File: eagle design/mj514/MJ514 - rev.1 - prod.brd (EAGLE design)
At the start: 49 x 18 mm, 14 parts, among them IC202 LDK320AM33R, IC302 STM32F042G6U6, IC401 TCAN334

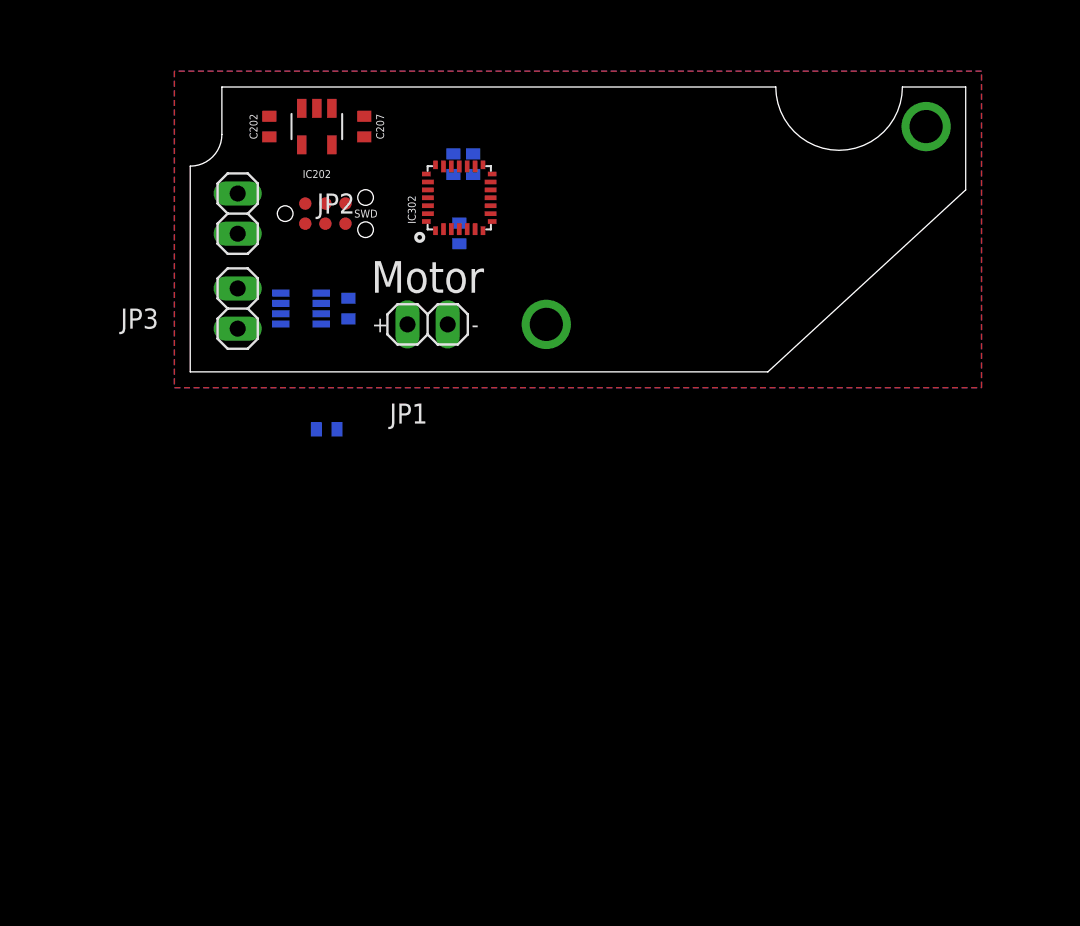
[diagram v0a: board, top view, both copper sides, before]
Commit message: MJ818 SuperNova Mini2: - added position key into PCB and spacers; updated gerber, dwg and stl
mj513 - grip:
- corrected bushing dimensions

in mj8x8-foo:
- minor corrections

general board-wide effort:
- replaced pinhead with 0.9mm TH
- added 2nd CAN H & L solder contact
- unified sch nets and drawings

in mj8x8 foo:
- developed rev.1b mj-foo device with voltage detector and CAN TVS protection

in mj808 design:
- updated front led shunt resistor to 0.18 Ohm

in mj8x8:
- added HR30-6R-6P - PushPull Receptacle.lbr receptable
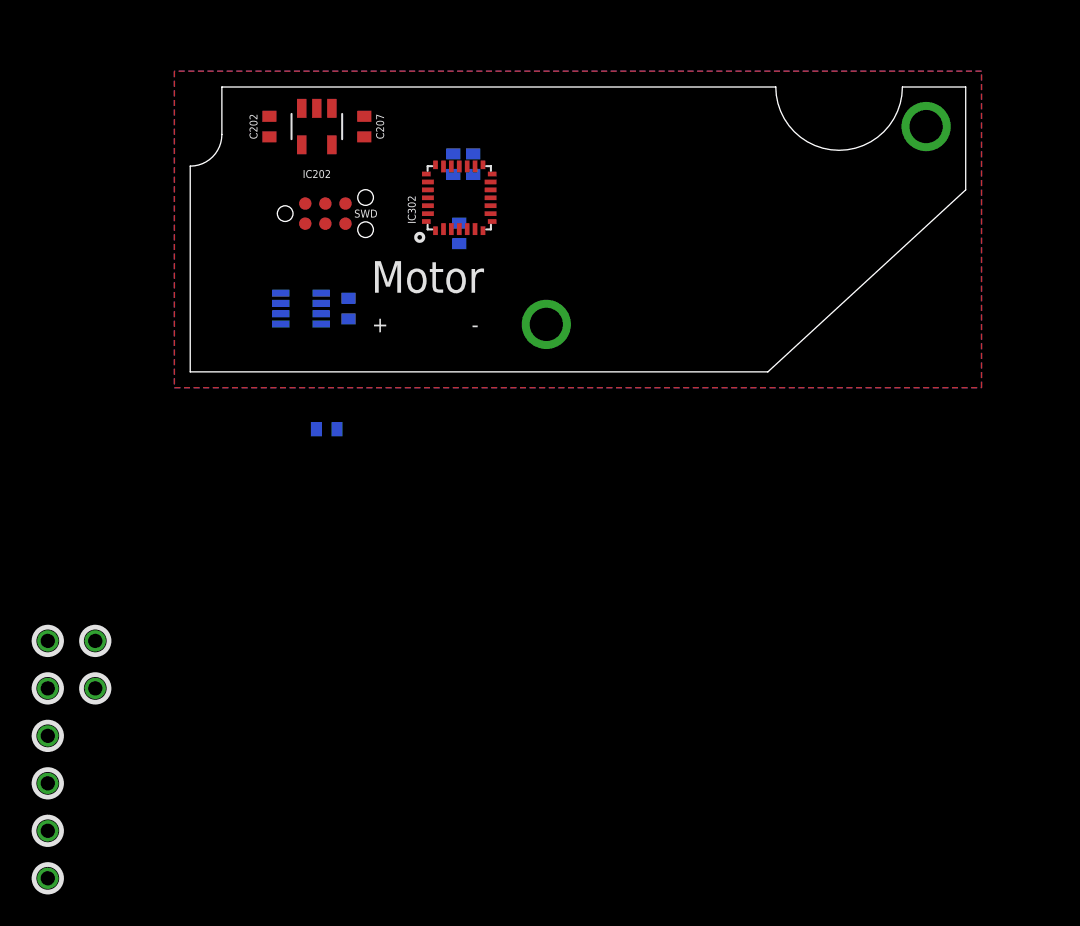
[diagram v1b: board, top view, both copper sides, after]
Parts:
- removed JP1, JP2, JP3: (no value), pinhead:1X02
- added TP1: LiIon + Terminal, signal testpoint:TH-0.9
- added TP2: LiIon - Terminal, signal testpoint:TH-0.9
- added TP3: motor +, signal testpoint:TH-0.9
- added TP4: motor -, signal testpoint:TH-0.9
- added TP5, TP7: CAN high, signal testpoint:TH-0.9
- added TP6, TP8: CAN low, signal testpoint:TH-0.9
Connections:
- net BAT+: now also TP1.P$1; no longer JP2.2
- net CAN_H: now also TP5.P$1, TP7.P$1; no longer JP3.1
- net CAN_L: now also TP6.P$1, TP8.P$1; no longer JP3.2
- net GND: now also TP2.P$1; no longer JP2.1
- net MOTOR+: now also TP3.P$1; no longer JP1.1
- net MOTOR-: now also TP4.P$1; no longer JP1.2
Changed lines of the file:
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@@
 </variantdefs>
 <classes>
-<class number="0" name="GND" width="0" drill="0">
+<class number="0" name="GND" width="0.25" drill="0.35">
+<clearance class="0" value="0.19"/>
 </class>
 <class number="1" name="BAT+" width="0.5" drill="0.35">
@@
 <attribute name="VALUE" x="7" y="4" size="0.5" layer="28" font="vector" rot="MR0" align="center"/>
 </element>
-<element name="JP1" library="pinhead" library_urn="urn:adsk.eagle:library:325" package="1X02" package3d_urn="urn:adsk.eagle:package:22435/2" value="" x="15" y="3" smashed="yes">
-<attribute name="NAME" x="15" y="-2" size="1.27" layer="25" ratio="10" rot="R180"/>
-<attribute name="POPULARITY" value="98" x="15" y="3" size="1.778" layer="27" display="off"/>
-<attribute name="VALUE" x="12.46" y="-0.175" size="1.27" layer="27"/>
-</element>
-<element name="JP2" library="pinhead" library_urn="urn:adsk.eagle:library:325" package="1X02" package3d_urn="urn:adsk.eagle:package:22435/2" value="" x="3" y="10" smashed="yes" rot="R90">
-<attribute name="NAME" x="8" y="10" size="1.27" layer="25" ratio="10"/>
-<attribute name="POPULARITY" value="98" x="3" y="10" size="1" layer="27" font="vector" rot="R90" display="off"/>
-<attribute name="VALUE" x="6.175" y="7.46" size="1.27" layer="27" rot="R90"/>
-</element>
-<element name="JP3" library="pinhead" library_urn="urn:adsk.eagle:library:325" package="1X02" package3d_urn="urn:adsk.eagle:package:22435/2" value="" x="3" y="4" smashed="yes" rot="R270">
-<attribute name="NAME" x="-2" y="4" size="1.27" layer="25" ratio="10" rot="R180"/>
-<attribute name="POPULARITY" value="98" x="3" y="4" size="1" layer="27" font="vector" rot="R270" display="off"/>
-<attribute name="VALUE" x="-0.175" y="6.54" size="1.27" layer="27" rot="R270"/>
-</element>
 <element name="SWD1" library="tag-connect" package="TC2030-NL" value="" x="6" y="10" smashed="yes"/>
+<element name="TP5" library="signal testpoint" package="TH-0.9" value="CAN high" x="-9" y="-17" smashed="yes"/>
+<element name="TP6" library="signal testpoint" package="TH-0.9" value="CAN low" x="-6" y="-17" smashed="yes"/>
+<element name="TP7" library="signal testpoint" package="TH-0.9" value="CAN high" x="-9" y="-20" smashed="yes"/>
+<element name="TP8" library="signal testpoint" package="TH-0.9" value="CAN low" x="-6" y="-20" smashed="yes"/>
+<element name="TP2" library="signal testpoint" package="TH-0.9" value="LiIon - Terminal" x="-9" y="-26" smashed="yes"/>
+<element name="TP1" library="signal testpoint" package="TH-0.9" value="LiIon + Terminal" x="-9" y="-23" smashed="yes"/>
+<element name="TP3" library="signal testpoint" package="TH-0.9" value="motor +" x="-9" y="-29" smashed="yes"/>
+<element name="TP4" library="signal testpoint" package="TH-0.9" value="motor -" x="-9" y="-32" smashed="yes"/>
 </elements>
 <signals>
@@
 <via x="22.5" y="3" extent="1-16" drill="2.1"/>
 <via x="46.5" y="15.5" extent="1-16" drill="2.1"/>
-<contactref element="JP2" pad="1"/>
 <contactref element="SWD1" pad="5_GND"/>
-<wire x1="17" y1="9.4" x2="9.275" y2="-3.625" width="0" layer="19" extent="1-1"/>
-<wire x1="16.625" y1="12.475" x2="17" y2="9.4" width="0" layer="19" extent="1-1"/>
-<wire x1="17.875" y1="12.475" x2="16.625" y2="12.475" width="0" layer="19" extent="1-1"/>
-<wire x1="8.275" y1="4.325" x2="17.875" y2="12.475" width="0" layer="19" extent="1-16"/>
-<wire x1="10" y1="4.65" x2="8.275" y2="4.325" width="0" layer="19" extent="16-16"/>
-<wire x1="9.81" y1="9.365" x2="8.275" y2="4.325" width="0" layer="19" extent="1-16"/>
+<contactref element="TP2" pad="P$1"/>
+<wire x1="22.5" y1="3" x2="46.5" y2="15.5" width="0" layer="19" extent="1-1"/>
+<wire x1="17" y1="9.4" x2="22.5" y2="3" width="0" layer="19" extent="16-16"/>
+<wire x1="16.625" y1="12.475" x2="17" y2="9.4" width="0" layer="19" extent="16-16"/>
+<wire x1="17.875" y1="12.475" x2="16.625" y2="12.475" width="0" layer="19" extent="16-16"/>
+<wire x1="18" y1="12.98" x2="17.875" y2="12.475" width="0" layer="19" extent="1-16"/>
+<wire x1="11" y1="16.15" x2="16.625" y2="12.475" width="0" layer="19" extent="1-16"/>
+<wire x1="8" y1="16.65" x2="11" y2="16.15" width="0" layer="19" extent="1-1"/>
+<wire x1="5" y1="14.85" x2="8" y2="16.65" width="0" layer="19" extent="1-1"/>
+<wire x1="9.81" y1="9.365" x2="11" y2="16.15" width="0" layer="19" extent="1-1"/>
+<wire x1="10" y1="4.65" x2="9.81" y2="9.365" width="0" layer="19" extent="1-16"/>
+<wire x1="8.275" y1="4.325" x2="10" y2="4.65" width="0" layer="19" extent="16-16"/>
+<wire x1="9.275" y1="-3.625" x2="8.275" y2="4.325" width="0" layer="19" extent="16-16"/>
+<wire x1="-9" y1="-26" x2="9.275" y2="-3.625" width="0" layer="19" extent="16-16"/>
 </signal>
 <signal name="BAT+" class="1">
@@
 <contactref element="IC202" pad="IN"/>
 <contactref element="C202" pad="1"/>
-<contactref element="JP2" pad="2"/>
-<wire x1="7.05" y1="16.65" x2="8.95" y2="16.65" width="0" layer="19" extent="1-1"/>
-<wire x1="5" y1="16.15" x2="7.05" y2="16.65" width="0" layer="19" extent="1-1"/>
-<wire x1="3" y1="11.27" x2="5" y2="16.15" width="0" layer="19" extent="1-1"/>
+<contactref element="TP1" pad="P$1"/>
+<wire x1="5" y1="16.15" x2="-9" y2="-23" width="0" layer="19" extent="1-1"/>
+<wire x1="7.05" y1="16.65" x2="5" y2="16.15" width="0" layer="19" extent="1-1"/>
+<wire x1="8.95" y1="16.65" x2="7.05" y2="16.65" width="0" layer="19" extent="1-1"/>
 </signal>
 <signal name="CAN_H" class="3">
 <contactref element="IC401" pad="P$7"/>
-<contactref element="JP3" pad="1"/>
-<wire x1="3" y1="5.27" x2="5.725" y2="4.325" width="0" layer="19" extent="16-16"/>
+<contactref element="TP5" pad="P$1"/>
+<contactref element="TP7" pad="P$1"/>
+<wire x1="-9" y1="-17" x2="-9" y2="-20" width="0" layer="19" extent="1-1"/>
+<wire x1="5.725" y1="4.325" x2="-9" y2="-17" width="0" layer="19" extent="16-16"/>
 </signal>
 <signal name="CAN_L" class="3">
 <contactref element="IC401" pad="P$6"/>
-<contactref element="JP3" pad="2"/>
-<wire x1="3" y1="2.73" x2="5.725" y2="3.675" width="0" layer="19" extent="16-16"/>
+<contactref element="TP8" pad="P$1"/>
+<contactref element="TP6" pad="P$1"/>
+<wire x1="-6" y1="-17" x2="-6" y2="-20" width="0" layer="19" extent="1-1"/>
+<wire x1="5.725" y1="3.675" x2="-6" y2="-17" width="0" layer="19" extent="16-16"/>
 </signal>
 <signal name="3V3" class="4">
+<contactref element="C405" pad="1"/>
+<contactref element="IC401" pad="P$3"/>
 <contactref element="IC202" pad="OUT"/>
 <contactref element="C207" pad="2"/>
@@
 <contactref element="C304" pad="2"/>
 <contactref element="C305" pad="2"/>
-<contactref element="C405" pad="1"/>
-<contactref element="IC401" pad="P$3"/>
 <contactref element="SWD1" pad="1_TVCC"/>
-<wire x1="16.625" y1="13.775" x2="17" y2="8.1" width="0" layer="19" extent="1-1"/>
-<wire x1="17.875" y1="13.775" x2="16.625" y2="13.775" width="0" layer="19" extent="1-1"/>
-<wire x1="10" y1="3.35" x2="17.875" y2="13.775" width="0" layer="19" extent="1-16"/>
-<wire x1="8.275" y1="3.675" x2="10" y2="3.35" width="0" layer="19" extent="16-16"/>
-<wire x1="7.27" y1="9.365" x2="8.275" y2="3.675" width="0" layer="19" extent="1-16"/>
-<wire x1="8.95" y1="14.35" x2="7.27" y2="9.365" width="0" layer="19" extent="1-1"/>
-<wire x1="11" y1="14.85" x2="8.95" y2="14.35" width="0" layer="19" extent="1-1"/>
-<wire x1="17" y1="12.98" x2="11" y2="14.85" width="0" layer="19" extent="1-1"/>
-<wire x1="17.5" y1="12.98" x2="17" y2="12.98" width="0" layer="19" extent="1-1"/>
+<wire x1="17.5" y1="12.98" x2="17.875" y2="13.775" width="0" layer="19" extent="1-16"/>
+<wire x1="17" y1="12.98" x2="17.5" y2="12.98" width="0" layer="19" extent="1-1"/>
+<wire x1="16.625" y1="13.775" x2="17" y2="12.98" width="0" layer="19" extent="1-16"/>
 <wire x1="17.5" y1="9.02" x2="17.5" y2="12.98" width="0" layer="19" extent="1-1"/>
+<wire x1="17" y1="8.1" x2="17.5" y2="9.02" width="0" layer="19" extent="1-16"/>
+<wire x1="11" y1="14.85" x2="16.625" y2="13.775" width="0" layer="19" extent="1-16"/>
+<wire x1="8.95" y1="14.35" x2="11" y2="14.85" width="0" layer="19" extent="1-1"/>
+<wire x1="7.27" y1="9.365" x2="8.95" y2="14.35" width="0" layer="19" extent="1-1"/>
+<wire x1="8.275" y1="3.675" x2="7.27" y2="9.365" width="0" layer="19" extent="1-16"/>
+<wire x1="10" y1="3.35" x2="8.275" y2="3.675" width="0" layer="19" extent="16-16"/>
 </signal>
 <signal name="SYS_SWDIO" class="3">
@@
 </polygon>
 </signal>
-<signal name="MOTOR+">
-<contactref element="JP1" pad="1"/>
-</signal>
-<signal name="MOTOR-">
-<contactref element="JP1" pad="2"/>
+<signal name="MOTOR+" class="5">
+<contactref element="TP3" pad="P$1"/>
+</signal>
+<signal name="MOTOR-" class="5">
+<contactref element="TP4" pad="P$1"/>
 </signal>
 </signals>

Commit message: mj514 prod work: - essentially copied POC sch & brd - added SHT40-AD1F - Humidity Sensor to POC and prod boards - converted to 6 layer board - ERC & DRC check out ok - created gerbers
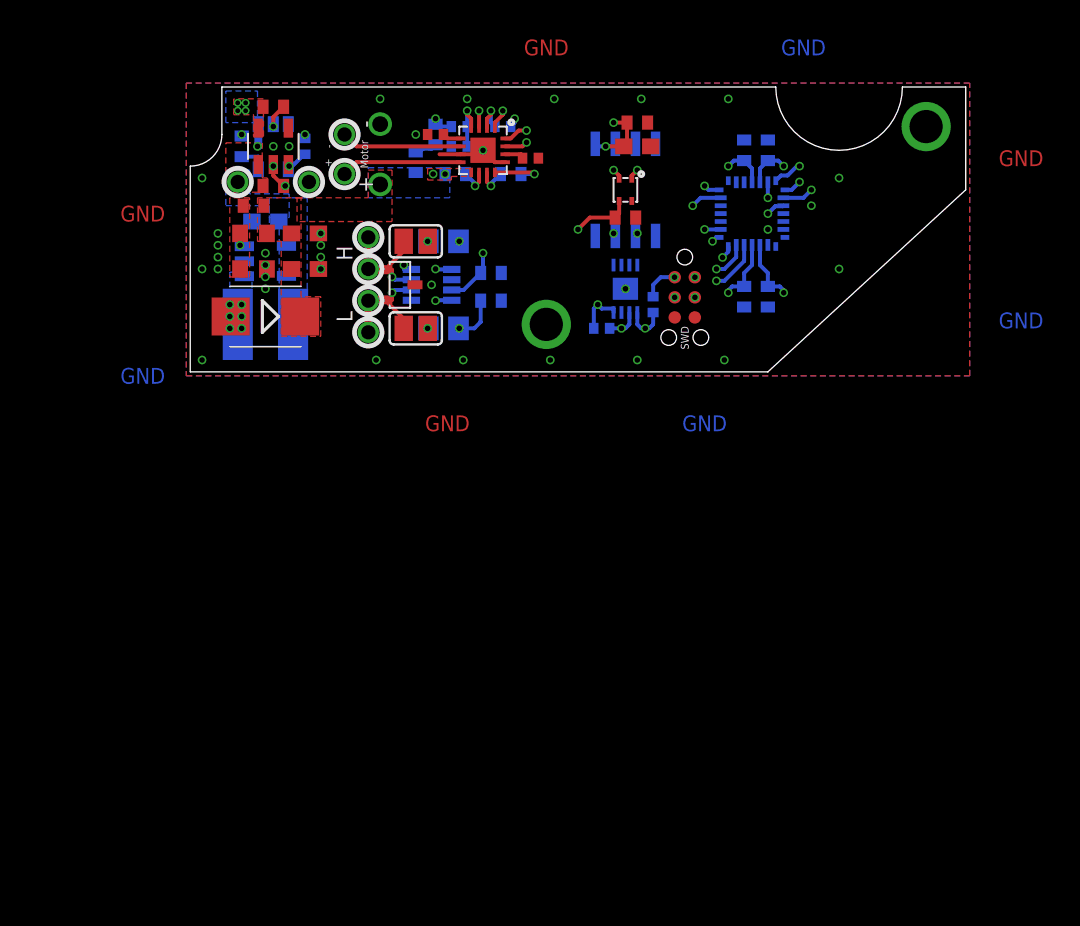
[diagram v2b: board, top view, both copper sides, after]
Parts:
- removed C202, C207: 1uF / 10V, rcl:C0402
- removed IC202: LDK320AM33R, LDK320 5V LDO:SOT-23-5L
- added C201, C203, C204, C701: 1uF / 10V, rcl:C0402
- added C402: 47nF / 10V, rcl:C0402
- added C501, C902, C903, C904: 0.1uF / 100V, rcl:C0402
- added C702, C801, C804: 10uF / 35V, rcl:C0603
- added C802: 4.7uF / 50V, rcl:C0603
- added C803: 68pF / 50V, rcl:C0402
- added C901: 22nF / 50V, rcl:C0402
- added C906: 100uF / 25V, C-Pol:TH
- added D801: MBRM120LT3G, diode:SMB
- added IC201: LDK320AM33R, LDK320 5V LDO:SOT-23-5L
- added IC203: R3119N058A-TR-FE, R3119x - Input Voltage Detector:SOT23-5
- added IC402: SZNUP2105LT1G, NUP2105L - 27V ESD Protection Diode:SOT-23-3
- added IC501: SHT40-AD1F-R2, SHT40-AD1F - Humidity Sensor:SMD
- added IC601: MB85RC16PN-G-AMERE1, MB85RC - FeRAM, I2C:SON-8
- added IC701: AS5601-ASOM, AS5601 - Programmable Contactless Encoder:SOIC8
- added IC801: LT1935ES5#TRMPBF, LTC1935 - Boost DC-DC Converter:TSOT-23-5
- added IC901: DRV8876RGTR, DRV8876 - H-Bridge Motor Driver:VQFN16
- added L801: CDRH4D18NP-4R7NC, CDRH4D18 - Power Inductor:5050
- added R1, R2: 4k7, rcl:R0402
- added R201: 100k, rcl:R0402
- added R402, R403: 60R, 0.5W, rcl:R0805
- added R801: 10k, rcl:R0603
- added R802: 85.6k, rcl:R0603
- added R901, R902: foo, rcl:R0402
- added R903: 10k, rcl:R0402
- added R905: 2.2k, rcl:R0402
- added R906: 1k, rcl:R0402
- added SJ401: CAN H term., jumper:SJ
- added SJ402: CAN L term., jumper:SJ
- C301, C305, C307, C405: value 0.1uF / 10V -> 0.1uF / 100V
- TP3: value motor + -> CAN high
- TP4: value motor - -> CAN high
- TP5: value CAN high -> CAN low
- TP7: value CAN high -> motor +
- TP8: value CAN low -> motor -
- moved TP4 45.3 mm to (11.2, 8.50), turned to 90 degrees
- moved TP2 41.4 mm to (7.50, 12.0), turned to 180 degrees
- moved TP3 40.9 mm to (11.2, 6.50), turned to 90 degrees
- moved TP7 39.7 mm to (9.75, 15.0)
- moved TP1 37.0 mm to (3.00, 12.0), turned to 180 degrees
- moved TP8 36.1 mm to (9.75, 12.5)
- moved C307 31.7 mm to (35.0, 14.0), turned to 270 degrees
- moved TP5 28.1 mm to (11.2, 2.50), turned to 90 degrees
- moved TP6 27.6 mm to (11.2, 4.50), turned to 90 degrees
- moved SWD1 25.4 mm to (31.2, 7.25), turned to 270 degrees
- moved C301 20.4 mm to (36.5, 4.75)
- moved C304 20.2 mm to (36.5, 14.0)
- moved C305 20.2 mm to (35.0, 4.75)
- moved IC302 18.5 mm to (35.5, 10.0), flipped to the bottom, turned to 270 degrees
- moved C405 9.28 mm to (19.0, 6.25), turned to 180 degrees
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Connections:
- new net 12V: C801.1, C803.1, C804.1, C902.2, C903.2, C906.POS, D801.C, IC901.P$9, R802.2
- new net 12V0:FB: C803.2, IC801.FB, R801.2, R802.1
- new net 12V0:SW: D801.A, IC801.SW, L801.P$2
- new net CAN_INFRA:H: R403.2, SJ401.2
- new net CAN_INFRA:L: R402.1, SJ402.2
- new net CAN_INFRA:SPLIT: C402.1, R402.2, R403.1
- new net FE-RAM:WP: IC601.P$7
- new net I2C_SCL: IC302.27_PB6, IC501.SCL, IC601.P$6, IC701.P$7, R1.1
- new net I2C_SDA: IC302.28_PB7, IC501.SDA, IC601.P$5, IC701.P$6, R2.1
- new net MC:CPH: C901.1, IC901.P$11
- new net MC:CPL: C901.2, IC901.P$12
- new net MC:IMODE: IC901.P$5, R901.2
- new net MC:IPROPI: IC901.P$4, R905.2, R906.2
- new net MC:PMODE: IC901.P$14, R902.2
- new net MC:VCP: C902.1, IC901.P$10
- new net MOTOR_FLT: IC302.8_PA2, IC901.P$2, R903.1
- new net MOTOR_IN1: IC302.6_PA0, IC901.P$15
- new net MOTOR_IN2: IC302.7_PA1, IC901.P$16
- new net MOTOR_IPROP: C904.1, IC302.10_PA4, R905.1
- new net MOTOR_SLP: IC302.9_PA3, IC901.P$1
- new net POWER_3V3:CD: C204.1, IC203.5_CD
- new net POWER_3V3:EN: IC201.EN, IC203.4_DOUT, R201.2
- new net ROTARYENCODER:A: IC701.P$8
- new net ROTARYENCODER:B: IC701.P$5
- new net ROTARYENCODER:PUSH: IC701.P$3
- new net STM32F04:PA5: IC302.11_PA5
- new net STM32F04:PA6: IC302.12_PA6
- new net STM32F04:PA7: IC302.13_PA7
- new net STM32F04:PB0: IC302.14_PB0
- new net STM32F04:PB1: IC302.15_PB1
- new net STM32F04:PB3: IC302.24_PB3
- new net STM32F04:PB4: IC302.25_PB4
- new net STM32F04:PB5: IC302.26_PB5
- new net STM32F04:PB8: IC302.1_PB8
- new net STM32F04:PF0: IC302.2_PF0
- new net STM32F04:PF1: IC302.3_PF1
- net 3V3: now also C203.2, C501.1, C701.1, C702.1, IC201.OUT, IC501.VDD, IC601.P$8, IC701.P$1, IC701.P$2, IC901.P$3, R1.2, R2.2, R903.2; no longer C207.2, IC202.OUT
- net BAT+: now also C201.1, C802.2, IC201.IN, IC203.1_VDD, IC801.!SHDN!, IC801.VIN, L801.P$1, R201.1; no longer C202.1, IC202.EN, IC202.IN
- net CAN_H: now also IC402.1, SJ401.1, TP3.P$1, TP4.P$1; no longer TP5.P$1, TP7.P$1
- net CAN_L: now also IC402.2, SJ402.1, TP5.P$1; no longer TP8.P$1
- net GND: now also C201.2, C203.1, C204.2, C402.2, C501.2, C701.2, C702.2, C801.2, C802.1, C804.2, C903.1, C904.2, C906.NEG, IC201.GND, IC203.2_GND, IC203.3_GND, IC402.3, IC501.VSS, IC601.P$1, IC601.P$2, IC601.P$3, IC601.P$4, IC601.P$9, IC701.P$4, IC801.GND, IC901.P$13, IC901.P$17, IC901.P$7, R801.1, R901.1, R902.1, R906.1; no longer C202.2, C207.1, IC202.GND
- net MOTOR+: now also IC901.P$6, TP7.P$1; no longer TP3.P$1
- net MOTOR-: now also IC901.P$8, TP8.P$1; no longer TP4.P$1
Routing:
- net MC:IPROPI: track 0.00 -> 33.0 mm, vias 0 -> 2
- net 3V3: track 0.00 -> 31.6 mm, vias 0 -> 15
- net MOTOR_FLT: track 0.00 -> 28.5 mm, vias 0 -> 2
- net MOTOR_IPROP: track 0.00 -> 27.3 mm, vias 0 -> 2
- net MOTOR_SLP: track 0.00 -> 25.5 mm, vias 0 -> 2
- net CAN_RX: track 0.00 -> 24.2 mm, vias 0 -> 2
- net !STBY!: track 0.00 -> 23.6 mm, vias 0 -> 2
- net CAN_TX: track 0.00 -> 23.1 mm, vias 0 -> 2
- net MOTOR_IN2: track 0.00 -> 22.7 mm, vias 0 -> 2
- net I2C_SCL: track 0.00 -> 21.4 mm, vias 0 -> 4
- net MOTOR_IN1: track 0.00 -> 20.3 mm, vias 0 -> 2
- net I2C_SDA: track 0.00 -> 19.5 mm, vias 0 -> 4
- net SYS_NRST: track 0.00 -> 15.2 mm, vias 0 -> 2
- net SYS_SWCLK: track 0.00 -> 11.7 mm, vias 0 -> 2
- net GND: track 0.00 -> 9.04 mm, vias 2 -> 40
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- added copper zone on layer 1, net 12V
- added copper zone on layer 16, net 12V
- added copper zone on layer 1, net 12V0:FB
- added copper zone on layer 16, net 12V0:SW
- added copper zone on layer 1, net 3V3
- added copper zone on layer 2, net 3V3
- added copper zone on layer 1, net BAT+
- added copper zone on layer 16, net BAT+
- added copper zone on layer 14, net EX
- added copper zone on layer 15, net EX
- added copper zone on layer 16, net EX
- added copper zone on layer 2, net EX
- added copper zone on layer 3, net EX
- added copper zone on layer 14, net GND
- added copper zone on layer 15, net GND
- added copper zone on layer 16, net GND
- added copper zone on layer 2, net GND
- added copper zone on layer 3, net GND
- removed copper zone on layer 16, net GND1
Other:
- board text added: "3V3"
- board text added: "GND"
- board text added: "H"
- board text added: "L"
